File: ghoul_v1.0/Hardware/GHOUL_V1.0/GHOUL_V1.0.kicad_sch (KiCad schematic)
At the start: 39 parts, among them J1 XT30, J2 Conn_01x02, J3 Conn_01x02, M2 Motor_Servo, U1 LM1084-ADJ, U2 DS18S20, U3 Xbee, U4 TPS62133, U5 MS5607-02BA, U6 MAX-M10S, U7 Teensy4.1

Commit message: akemi testing git
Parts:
- MOSFET2: footprint Package_TO_SOT_SMD:TO-252-2 -> Package_TO_SOT_SMD:SOT-23-6
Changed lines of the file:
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@@
 			)
 		)
-		(property "Footprint" "Package_TO_SOT_SMD:TO-252-2"
+		(property "Footprint" "Package_TO_SOT_SMD:SOT-23-6"
 			(at 198.12 92.075 0)
 			(effects

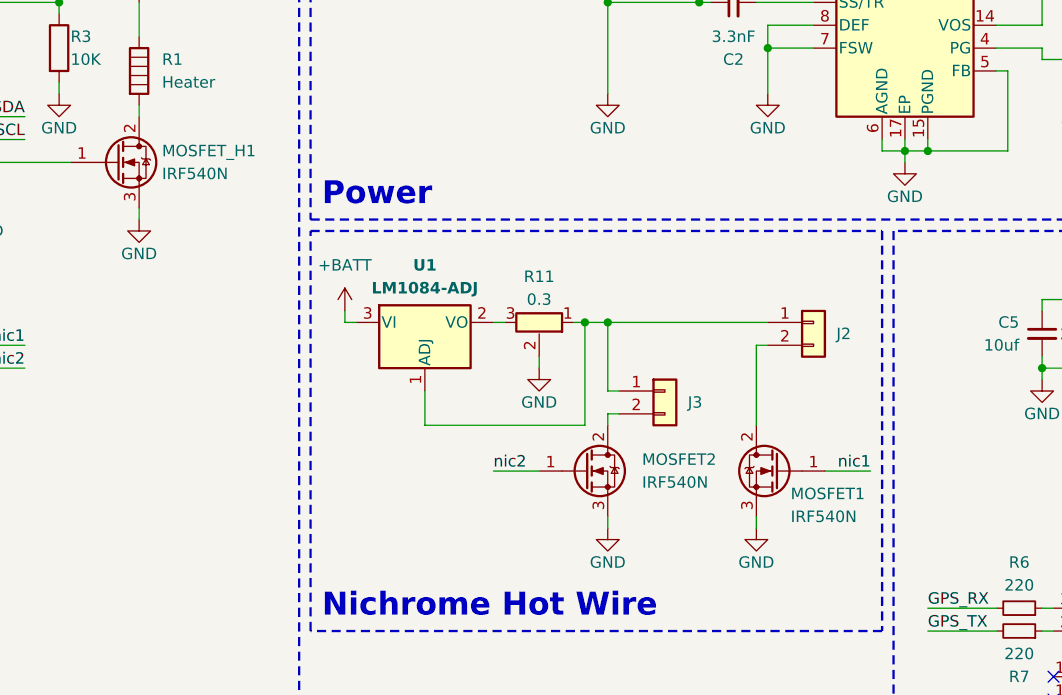
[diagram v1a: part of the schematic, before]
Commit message: correct BOM for ordering parts
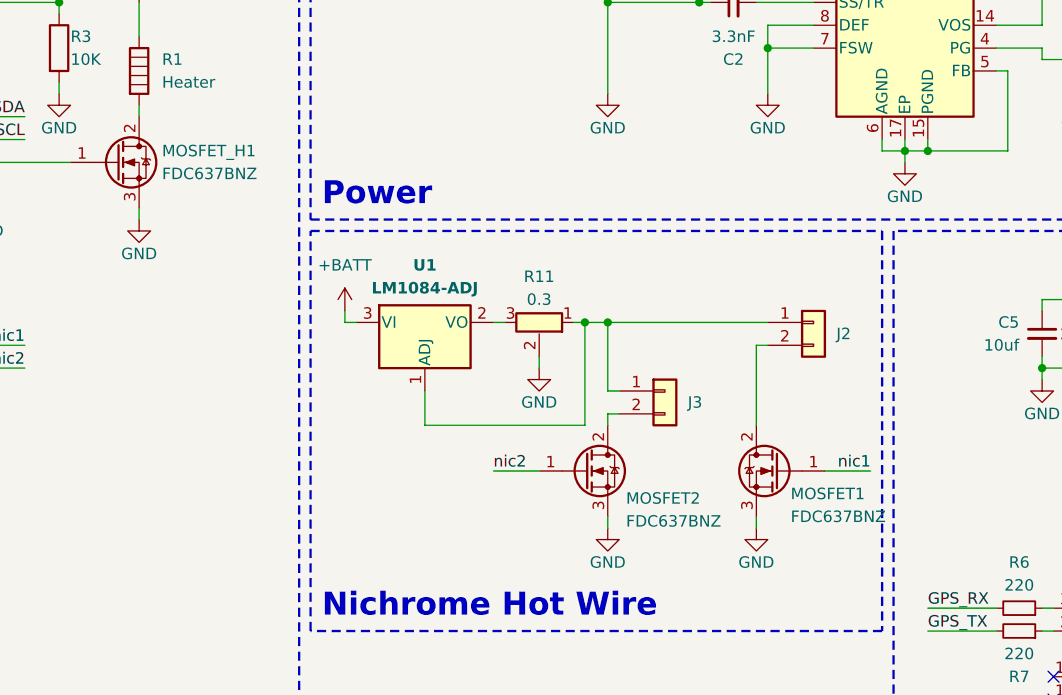
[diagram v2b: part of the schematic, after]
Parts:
- MOSFET1, MOSFET_H1: value IRF540N -> FDC637BNZ; footprint Package_TO_SOT_SMD:TO-252-2 -> Package_TO_SOT_SMD:SOT-23-6
- MOSFET2: value IRF540N -> FDC637BNZ
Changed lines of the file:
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@@
 		(on_board yes)
 		(dnp no)
-		(fields_autoplaced yes)
 		(property "Reference" "MOSFET2"
-			(at 198.12 88.8999 0)
+			(at 196.342 93.218 0)
 			(effects
 				(font
@@
 			)
 		)
-		(property "Value" "IRF540N"
-			(at 198.12 91.4399 0)
+		(property "Value" "FDC637BNZ"
+			(at 196.342 95.758 0)
 			(effects
 				(font
@@
 			)
 		)
-		(property "Datasheet" "http://www.irf.com/product-info/datasheets/data/irf540n.pdf"
+		(property "Datasheet" "https://www.onsemi.com/pdf/datasheet/fdc637bnz-d.pdf"
 			(at 191.77 90.17 0)
 			(effects
@@
 			)
 		)
-		(property "Value" "IRF540N"
+		(property "Value" "FDC637BNZ"
 			(at 144.78 57.15 0)
 			(effects
@@
 			)
 		)
-		(property "Footprint" "Package_TO_SOT_SMD:TO-252-2"
+		(property "Footprint" "Package_TO_SOT_SMD:SOT-23-6"
 			(at 146.05 57.785 0)
 			(effects
@@
 			)
 		)
-		(property "Datasheet" "http://www.irf.com/product-info/datasheets/data/irf540n.pdf"
+		(property "Datasheet" "https://www.onsemi.com/pdf/datasheet/fdc637bnz-d.pdf"
 			(at 139.7 55.88 0)
 			(effects
@@
 			)
 		)
-		(property "Value" "IRF540N"
+		(property "Value" "FDC637BNZ"
 			(at 214.63 95.25 0)
 			(effects
@@
 			)
 		)
-		(property "Footprint" "Package_TO_SOT_SMD:TO-252-2"
+		(property "Footprint" "Package_TO_SOT_SMD:SOT-23-6"
 			(at 207.01 92.075 0)
 			(effects
@@
 			)
 		)
-		(property "Datasheet" "http://www.irf.com/product-info/datasheets/data/irf540n.pdf"
+		(property "Datasheet" "https://www.onsemi.com/pdf/datasheet/fdc637bnz-d.pdf"
 			(at 213.36 90.17 0)
 			(effects

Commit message: final akemi changes
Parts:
- removed MOSFET1, MOSFET2, MOSFET_H1: FDC637BNZ, Package_TO_SOT_SMD:SOT-23-6, symbol Transistor_FET:IRF540N
- added Q1, Q2, Q3: FDC637BNZ, Package_TO_SOT_SMD:TSOT-23-6, symbol Transistor_FET:RQ6E080AJ
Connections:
- net GND: now also Q1.4 (S), Q2.4 (S), Q3.4 (S)
- net nic1: now also Q3.3 (G)
- net nic2: now also Q2.3 (G)
- net at U7.37 (15_A1_RX3_SPDIF_IN): now also Q1.3 (G)
- net at J3.2 (Pin_2): now also Q2.1 (D), Q2.2 (D), Q2.5 (D), Q2.6 (D)
- net at R1.2: now also Q1.1 (D), Q1.2 (D), Q1.5 (D), Q1.6 (D)
- net at J2.2 (Pin_2): now also Q3.1 (D), Q3.2 (D), Q3.5 (D), Q3.6 (D)
